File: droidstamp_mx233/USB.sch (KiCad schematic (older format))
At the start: 37 parts, among them J3 USB_2A, J4 USB-MINI, U4 GL850G, U5 RCLAMP0502B, U6 RCLAMP0502B, U7 RCLAMP0502B, U8 RCLAMP0502B, U9 FSUSB43, X2 12MHz

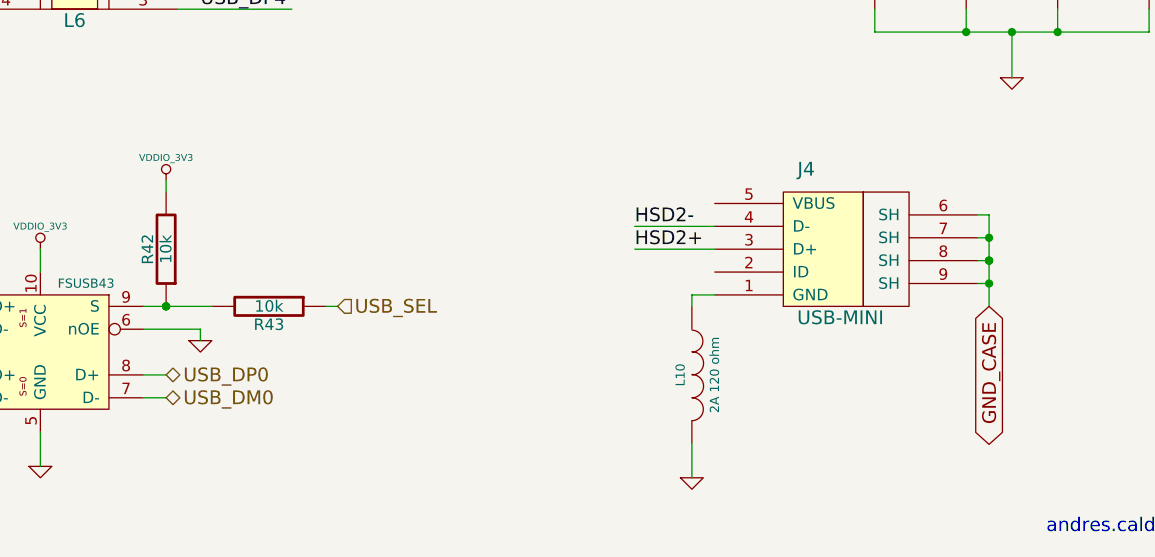
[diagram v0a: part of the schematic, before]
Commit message: TODO file added
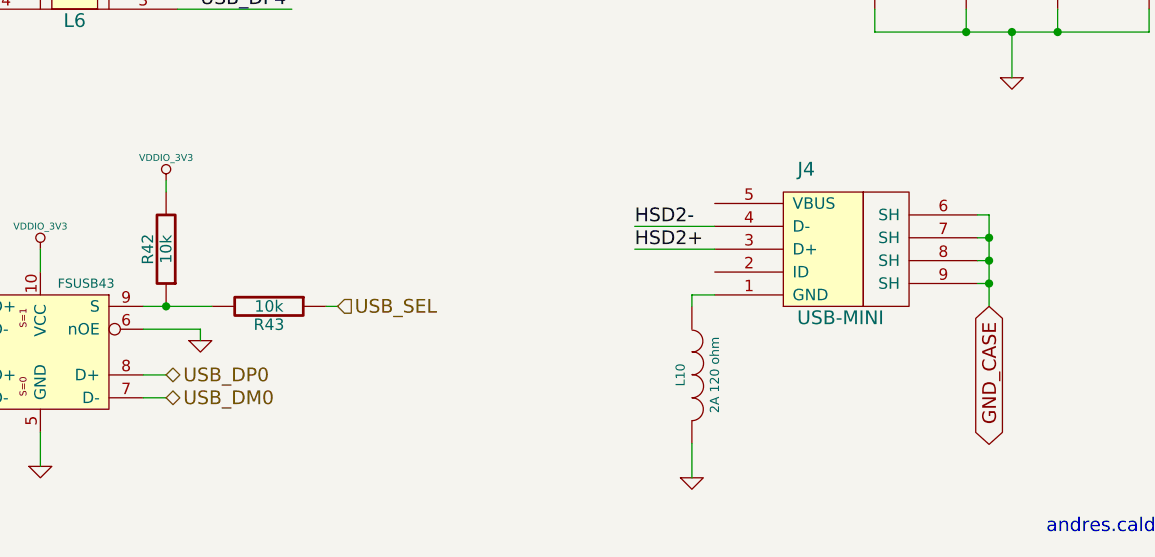
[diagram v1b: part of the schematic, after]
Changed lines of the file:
@@
-EESchema Schematic File Version 2  date mié 12 sep 2012 20:12:14 COT
+EESchema Schematic File Version 2  date Wed 03 Oct 2012 07:36:32 PM COT
 LIBS:con-jack
 LIBS:adm3101e
@@
 EELAYER 25  0
 EELAYER END
-$Descr A4 11700 8267
+$Descr A4 11693 8268
 encoding utf-8
 Sheet 5 5
 Title ""
-Date "13 sep 2012"
+Date "4 oct 2012"
 Rev ""
 Comp ""
@@
 $EndComp
 $Comp
-L GND #PWR0129
+L GND #PWR139
 U 1 1 4F522478
 P 6550 3850
-F 0 "#PWR0129" H 6550 3850 30  0001 C CNN
+F 0 "#PWR139" H 6550 3850 30  0001 C CNN
 F 1 "GND" H 6550 3780 30  0001 C CNN
 	1    6550 3850
@@
 USM_P2
 $Comp
-L VDDIO_3V3 #PWR0130
+L VDDIO_3V3 #PWR138
 U 1 1 4E5BAA82
 P 6500 1750
-F 0 "#PWR0130" H 6500 1850 30  0001 C CNN
+F 0 "#PWR138" H 6500 1850 30  0001 C CNN
 F 1 "VDDIO_3V3" H 6500 1850 30  0000 C CNN
 	1    6500 1750
@@
 $EndComp
 $Comp
-L GND #PWR0131
+L GND #PWR134
 U 1 1 4E43139E
 P 4950 3200
-F 0 "#PWR0131" H 4950 3200 30  0001 C CNN
+F 0 "#PWR134" H 4950 3200 30  0001 C CNN
 F 1 "GND" H 4950 3130 30  0001 C CNN
 	1    4950 3200
@@
 $EndComp
 $Comp
-L GND #PWR0132
+L GND #PWR140
 U 1 1 4E41C8A5
 P 6700 3350
-F 0 "#PWR0132" H 6700 3350 30  0001 C CNN
+F 0 "#PWR140" H 6700 3350 30  0001 C CNN
 F 1 "GND" H 6700 3280 30  0001 C CNN
 	1    6700 3350
@@
 $EndComp
 $Comp
-L GND #PWR0133
+L GND #PWR130
 U 1 1 4E4157F8
 P 3950 4850
-F 0 "#PWR0133" H 3950 4850 30  0001 C CNN
+F 0 "#PWR130" H 3950 4850 30  0001 C CNN
 F 1 "GND" H 3950 4780 30  0001 C CNN
 	1    3950 4850
@@
 $EndComp
 $Comp
-L GND #PWR0134
+L GND #PWR129
 U 1 1 4E4157E9
 P 3950 3800
-F 0 "#PWR0134" H 3950 3800 30  0001 C CNN
+F 0 "#PWR129" H 3950 3800 30  0001 C CNN
 F 1 "GND" H 3950 3730 30  0001 C CNN
 	1    3950 3800
@@
 $EndComp
 $Comp
-L GND #PWR0135
+L GND #PWR132
 U 1 1 4E4157C0
 P 4000 2650
-F 0 "#PWR0135" H 4000 2650 30  0001 C CNN
+F 0 "#PWR132" H 4000 2650 30  0001 C CNN
 F 1 "GND" H 4000 2580 30  0001 C CNN
 	1    4000 2650
@@
 $EndComp
 $Comp
-L GND #PWR0136
+L GND #PWR131
 U 1 1 4E4157B3
 P 4000 1350
-F 0 "#PWR0136" H 4000 1350 30  0001 C CNN
+F 0 "#PWR131" H 4000 1350 30  0001 C CNN
 F 1 "GND" H 4000 1280 30  0001 C CNN
 	1    4000 1350
@@
 $EndComp
 $Comp
-L GND #PWR0137
+L GND #PWR123
 U 1 1 4E415157
 P 1100 2050
-F 0 "#PWR0137" H 1100 2050 30  0001 C CNN
+F 0 "#PWR123" H 1100 2050 30  0001 C CNN
 F 1 "GND" H 1100 1980 30  0001 C CNN
 	1    1100 2050
@@
 $EndComp
 $Comp
-L GND #PWR0138
+L GND #PWR124
 U 1 1 4E414F30
 P 2400 2100
-F 0 "#PWR0138" H 2400 2100 30  0001 C CNN
+F 0 "#PWR124" H 2400 2100 30  0001 C CNN
 F 1 "GND" H 2400 2030 30  0001 C CNN
 	1    2400 2100
@@
 $EndComp
 $Comp
-L VDD5V #PWR0139
+L VDD5V #PWR122
 U 1 1 4E414E3D
 P 650 1150
-F 0 "#PWR0139" H 650 1250 30  0001 C CNN
+F 0 "#PWR122" H 650 1250 30  0001 C CNN
 F 1 "VDD5V" H 650 1250 30  0000 C CNN
 	1    650  1150
@@
 $EndComp
 $Comp
-L GND #PWR0140
+L GND #PWR142
 U 1 1 4E3C4430
 P 7400 1400
-F 0 "#PWR0140" H 7400 1400 30  0001 C CNN
+F 0 "#PWR142" H 7400 1400 30  0001 C CNN
 F 1 "GND" H 7400 1330 30  0001 C CNN
 	1    7400 1400
@@
 $EndComp
 $Comp
-L VDD5V #PWR0141
+L VDD5V #PWR141
 U 1 1 4E3C4429
 P 7400 800
-F 0 "#PWR0141" H 7400 900 30  0001 C CNN
+F 0 "#PWR141" H 7400 900 30  0001 C CNN
 F 1 "VDD5V" H 7400 900 30  0000 C CNN
 	1    7400 800
@@
 $EndComp
 $Comp
-L VDD5V #PWR0142
+L VDD5V #PWR146
 U 1 1 4E3C4418
 P 9000 2500
-F 0 "#PWR0142" H 9000 2600 30  0001 C CNN
+F 0 "#PWR146" H 9000 2600 30  0001 C CNN
 F 1 "VDD5V" H 9000 2600 30  0000 C CNN
 	1    9000 2500
@@
 $EndComp
 $Comp
-L GND #PWR0143
+L GND #PWR144
 U 1 1 4E3C436B
 P 7900 1600
-F 0 "#PWR0143" H 7900 1600 30  0001 C CNN
+F 0 "#PWR144" H 7900 1600 30  0001 C CNN
 F 1 "GND" H 7900 1530 30  0001 C CNN
 	1    7900 1600
@@
 USBH_P33V
 $Comp
-L VDD5V #PWR0144
+L VDD5V #PWR147
 U 1 1 4E3C4207
 P 9000 2900
-F 0 "#PWR0144" H 9000 3000 30  0001 C CNN
+F 0 "#PWR147" H 9000 3000 30  0001 C CNN
 F 1 "VDD5V" H 9000 3000 30  0000 C CNN
 	1    9000 2900
@@
 USBH_P33V
 $Comp
-L GND #PWR0145
+L GND #PWR148
 U 1 1 4E3C3A60
 P 9300 5550
-F 0 "#PWR0145" H 9300 5550 30  0001 C CNN
+F 0 "#PWR148" H 9300 5550 30  0001 C CNN
 F 1 "GND" H 9300 5480 30  0001 C CNN
 	1    9300 5550
@@
 $EndComp
 $Comp
-L GND #PWR0146
+L GND #PWR143
 U 1 1 4E3C3A56
 P 7400 5550
-F 0 "#PWR0146" H 7400 5550 30  0001 C CNN
+F 0 "#PWR143" H 7400 5550 30  0001 C CNN
 F 1 "GND" H 7400 5480 30  0001 C CNN
 	1    7400 5550
@@
 andres.calderon@emqbit.com\n
 $Comp
-L GND #PWR0147
+L GND #PWR136
 U 1 1 4E3C3807
 P 5900 2300
-F 0 "#PWR0147" H 5900 2300 30  0001 C CNN
+F 0 "#PWR136" H 5900 2300 30  0001 C CNN
 F 1 "GND" H 5900 2230 30  0001 C CNN
 	1    5900 2300
@@
 $EndComp
 $Comp
-L GND #PWR0148
+L GND #PWR149
 U 1 1 4E3C36BE
 P 9800 3550
-F 0 "#PWR0148" H 9800 3550 30  0001 C CNN
+F 0 "#PWR149" H 9800 3550 30  0001 C CNN
 F 1 "GND" H 9800 3480 30  0001 C CNN
 	1    9800 3550
@@
 X1
 $Comp
-L GND #PWR0149
+L GND #PWR145
 U 1 1 4E3C222B
 P 8900 3700
-F 0 "#PWR0149" H 8900 3700 30  0001 C CNN
+F 0 "#PWR145" H 8900 3700 30  0001 C CNN
 F 1 "GND" H 8900 3630 30  0001 C CNN
 	1    8900 3700
@@
 USB_DM2
 $Comp
-L GND #PWR0150
+L GND #PWR133
 U 1 1 4E3C212B
 P 4650 4250
-F 0 "#PWR0150" H 4650 4250 30  0001 C CNN
+F 0 "#PWR133" H 4650 4250 30  0001 C CNN
 F 1 "GND" H 4650 4180 30  0001 C CNN
 	1    4650 4250
@@
 $EndComp
 $Comp
-L GND #PWR0151
+L GND #PWR135
 U 1 1 4E3C206C
 P 5250 4250
-F 0 "#PWR0151" H 5250 4250 30  0001 C CNN
+F 0 "#PWR135" H 5250 4250 30  0001 C CNN
 F 1 "GND" H 5250 4180 30  0001 C CNN
 	1    5250 4250
@@
 $EndComp
 $Comp
-L GND #PWR0152
+L GND #PWR128
 U 1 1 502BA221
 P 3850 6700
-F 0 "#PWR0152" H 3850 6700 30  0001 C CNN
+F 0 "#PWR128" H 3850 6700 30  0001 C CNN
 F 1 "GND" H 3850 6630 30  0001 C CNN
 	1    3850 6700
@@
 HSD1-
 $Comp
-L VDDIO_3V3 #PWR0153
+L VDDIO_3V3 #PWR125
 U 1 1 502BB6BD
 P 3150 6300
-F 0 "#PWR0153" H 3150 6400 30  0001 C CNN
+F 0 "#PWR125" H 3150 6400 30  0001 C CNN
 F 1 "VDDIO_3V3" H 3150 6400 30  0000 C CNN
 	1    3150 6300
@@
 $EndComp
 $Comp
-L GND #PWR0154
+L GND #PWR126
 U 1 1 502BB9B6
 P 3150 7250
-F 0 "#PWR0154" H 3150 7250 30  0001 C CNN
+F 0 "#PWR126" H 3150 7250 30  0001 C CNN
 F 1 "GND" H 3150 7180 30  0001 C CNN
 	1    3150 7250
@@
 $EndComp
 $Comp
-L VDDIO_3V3 #PWR0155
+L VDDIO_3V3 #PWR127
 U 1 1 502BBDA2
 P 3700 6000
-F 0 "#PWR0155" H 3700 6100 30  0001 C CNN
+F 0 "#PWR127" H 3700 6100 30  0001 C CNN
 F 1 "VDDIO_3V3" H 3700 6100 30  0000 C CNN
 	1    3700 6000
@@
 $EndComp
 $Comp
-L GND #PWR0156
+L GND #PWR137
 U 1 1 502BD90C
 P 6000 7300
-F 0 "#PWR0156" H 6000 7300 30  0001 C CNN
+F 0 "#PWR137" H 6000 7300 30  0001 C CNN
 F 1 "GND" H 6000 7230 30  0001 C CNN
 	1    6000 7300
@@
 	3700 6050 3700 6000
 Connection ~ 3700 6550
-Connection ~ 3700 6550
 Wire Wire Line
 	6100 6300 5750 6300
@@
 	7250 6350 7300 6350
 Connection ~ 7300 6350
-Connection ~ 7300 6350
 Connection ~ 7300 6450
